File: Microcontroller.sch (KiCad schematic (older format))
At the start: 5 parts

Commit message: added jtag programming header for uC
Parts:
- added J?: Conn_02x03_Counter_Clockwise, symbol Connector_Generic:Conn_02x03_Counter_Clockwise
- added U?: STM32F446VET6-sternie, symbol engine_controller_series3-rescue:STM32F446VET6-sternie
- added U?: OSCILLATOR-sternie, symbol engine_controller_series3-rescue:OSCILLATOR-sternie
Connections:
- net labels added: +3V3, GND, NRST, SW0, SWCLK, SWDIO
- wire segments 15 -> 23
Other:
- note added: "Programming Header\n"
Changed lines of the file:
@@
 EESchema Schematic File Version 4
-LIBS:bangbang_rev1-cache
 EELAYER 30 0
 EELAYER END
 $Descr A4 11693 8268
 encoding utf-8
-Sheet 5 10
+Sheet 7 10
 Title ""
 Date ""
@@
 L engine_controller_series3-rescue:STM32F446VET6-sternie U?
 U 1 1 5E534371
-P 2850 1950
-F 0 "U?" H 2458 2213 49  0000 C CNN
-F 1 "STM32F446VET6-sternie" H 2458 2123 49  0000 C CNN
-F 2 "" H 2000 1000 49  0001 C CNN
-F 3 "" H 2000 1000 49  0001 C CNN
-	1    2850 1950
+P 1750 1300
+F 0 "U?" H 1358 1563 49  0000 C CNN
+F 1 "STM32F446VET6-sternie" H 1358 1473 49  0000 C CNN
+F 2 "" H 900 350 49  0001 C CNN
+F 3 "" H 900 350 49  0001 C CNN
+	1    1750 1300
 	1    0    0    -1
 $EndComp
@@
 L engine_controller_series3-rescue:STM32F446VET6-sternie U?
 U 2 1 5E53758A
-P 5400 2000
-F 0 "U?" H 5033 2263 49  0000 C CNN
-F 1 "STM32F446VET6-sternie" H 5033 2173 49  0000 C CNN
-F 2 "" H 4550 1050 49  0001 C CNN
-F 3 "" H 4550 1050 49  0001 C CNN
-	2    5400 2000
+P 4300 1350
+F 0 "U?" H 3933 1613 49  0000 C CNN
+F 1 "STM32F446VET6-sternie" H 3933 1523 49  0000 C CNN
+F 2 "" H 3450 400 49  0001 C CNN
+F 3 "" H 3450 400 49  0001 C CNN
+	2    4300 1350
 	1    0    0    -1
 $EndComp
@@
 L engine_controller_series3-rescue:STM32F446VET6-sternie U?
 U 3 1 5E53B3C0
-P 2950 4450
-F 0 "U?" H 2483 4713 49  0000 C CNN
-F 1 "STM32F446VET6-sternie" H 2483 4623 49  0000 C CNN
-F 2 "" H 2100 3500 49  0001 C CNN
-F 3 "" H 2100 3500 49  0001 C CNN
-	3    2950 4450
+P 1850 3800
+F 0 "U?" H 1383 4063 49  0000 C CNN
+F 1 "STM32F446VET6-sternie" H 1383 3973 49  0000 C CNN
+F 2 "" H 1000 2850 49  0001 C CNN
+F 3 "" H 1000 2850 49  0001 C CNN
+	3    1850 3800
 	1    0    0    -1
 $EndComp
@@
 L engine_controller_series3-rescue:STM32F446VET6-sternie U?
 U 4 1 5E53EB96
-P 5300 4400
-F 0 "U?" H 5008 4663 49  0000 C CNN
-F 1 "STM32F446VET6-sternie" H 5008 4573 49  0000 C CNN
-F 2 "" H 4450 3450 49  0001 C CNN
-F 3 "" H 4450 3450 49  0001 C CNN
-	4    5300 4400
+P 4200 3750
+F 0 "U?" H 3908 4013 49  0000 C CNN
+F 1 "STM32F446VET6-sternie" H 3908 3923 49  0000 C CNN
+F 2 "" H 3350 2800 49  0001 C CNN
+F 3 "" H 3350 2800 49  0001 C CNN
+	4    4200 3750
 	1    0    0    -1
 $EndComp
@@
 L engine_controller_series3-rescue:STM32F446VET6-sternie U?
 U 5 1 5E54171C
-P 7550 1900
-F 0 "U?" H 7258 2163 49  0000 C CNN
-F 1 "STM32F446VET6-sternie" H 7258 2073 49  0000 C CNN
-F 2 "" H 6700 950 49  0001 C CNN
-F 3 "" H 6700 950 49  0001 C CNN
-	5    7550 1900
-	1    0    0    -1
-$EndComp
-Text GLabel 3050 2450 2    50   Input ~ 0
+P 6300 1400
+F 0 "U?" H 6008 1663 49  0000 C CNN
+F 1 "STM32F446VET6-sternie" H 6008 1573 49  0000 C CNN
+F 2 "" H 5450 450 49  0001 C CNN
+F 3 "" H 5450 450 49  0001 C CNN
+	5    6300 1400
+	1    0    0    -1
+$EndComp
+Text GLabel 1950 1800 2    50   Input ~ 0
 SPI1_SCK
-Text GLabel 3050 2550 2    50   Input ~ 0
+Text GLabel 1950 1900 2    50   Input ~ 0
 SPI1_MISO
-Text GLabel 3050 2650 2    50   Input ~ 0
+Text GLabel 1950 2000 2    50   Input ~ 0
 SPI1_MOSI
 Wire Wire Line
-	2850 2450 3050 2450
-Wire Wire Line
-	2850 2550 3050 2550
-Wire Wire Line
-	2850 2650 3050 2650
-Text GLabel 3050 2950 2    50   Input ~ 0
+	1750 1800 1950 1800
+Wire Wire Line
+	1750 1900 1950 1900
+Wire Wire Line
+	1750 2000 1950 2000
+Text GLabel 1950 2300 2    50   Input ~ 0
 en_vlv0
-Text GLabel 3050 3050 2    50   Input ~ 0
+Text GLabel 1950 2400 2    50   Input ~ 0
 en_vlv1
 Wire Wire Line
-	2850 2950 3050 2950
-Wire Wire Line
-	2850 3050 3050 3050
-Text GLabel 3150 5050 2    50   Input ~ 0
+	1750 2300 1950 2300
+Wire Wire Line
+	1750 2400 1950 2400
+Text GLabel 2050 4400 2    50   Input ~ 0
 Mtr1_pwm
 Wire Wire Line
-	3150 5050 2950 5050
-Text GLabel 5600 2300 2    50   Input ~ 0
+	2050 4400 1850 4400
+Text GLabel 4500 1650 2    50   Input ~ 0
 Mtr0_B_L
-Text GLabel 5600 2400 2    50   Input ~ 0
+Text GLabel 4500 1750 2    50   Input ~ 0
 Mtr0_B_H
-Text GLabel 5600 2500 2    50   Input ~ 0
+Text GLabel 4500 1850 2    50   Input ~ 0
 Mtr0_A_L
-Text GLabel 5600 2600 2    50   Input ~ 0
+Text GLabel 4500 1950 2    50   Input ~ 0
 Mtr0_A_H
 Wire Wire Line
-	5400 2300 5600 2300
-Wire Wire Line
-	5400 2400 5600 2400
-Wire Wire Line
-	5400 2500 5600 2500
-Wire Wire Line
-	5400 2600 5600 2600
-Text GLabel 5550 4500 2    50   Input ~ 0
+	4300 1650 4500 1650
+Wire Wire Line
+	4300 1750 4500 1750
+Wire Wire Line
+	4300 1850 4500 1850
+Wire Wire Line
+	4300 1950 4500 1950
+Text GLabel 4450 3850 2    50   Input ~ 0
 Mtr1_B_L
-Text GLabel 5550 4600 2    50   Input ~ 0
+Text GLabel 4450 3950 2    50   Input ~ 0
 Mtr1_B_H
-Text GLabel 5550 4700 2    50   Input ~ 0
+Text GLabel 4450 4050 2    50   Input ~ 0
 Mtr1_A_L
-Text GLabel 5550 4800 2    50   Input ~ 0
+Text GLabel 4450 4150 2    50   Input ~ 0
 Mtr1_A_H
 Wire Wire Line
-	5300 4500 5550 4500
-Wire Wire Line
-	5550 4600 5300 4600
-Wire Wire Line
-	5300 4700 5550 4700
-Wire Wire Line
-	5550 4800 5300 4800
-Text GLabel 7750 2800 2    50   Input ~ 0
+	4200 3850 4450 3850
+Wire Wire Line
+	4450 3950 4200 3950
+Wire Wire Line
+	4200 4050 4450 4050
+Wire Wire Line
+	4450 4150 4200 4150
+Text GLabel 6500 2300 2    50   Input ~ 0
 Mtr0_pwm
 Wire Wire Line
-	7550 2800 7750 2800
+	6300 2300 6500 2300
+Text Notes 7000 5400 0    123  ~ 25
+Programming Header\n
+$Comp
+L Connector_Generic:Conn_02x03_Counter_Clockwise J?
+U 1 1 5E5320E3
+P 7900 5950
+F 0 "J?" H 7950 6267 50  0000 C CNN
+F 1 "Conn_02x03_Counter_Clockwise" H 7950 6176 50  0000 C CNN
+F 2 "" H 7900 5950 50  0001 C CNN
+F 3 "~" H 7900 5950 50  0001 C CNN
+	1    7900 5950
+	1    0    0    -1
+$EndComp
+Text GLabel 8300 5850 2    50   Input ~ 0
+SW0
+Text GLabel 7550 5850 0    50   Input ~ 0
+SWDIO
+Text GLabel 7550 5950 0    50   Input ~ 0
+SWCLK
+Text GLabel 7550 6050 0    50   Input ~ 0
+NRST
+Wire Wire Line
+	7550 5850 7700 5850
+Wire Wire Line
+	7700 5950 7550 5950
+Wire Wire Line
+	7550 6050 7700 6050
+Wire Wire Line
+	8200 5850 8300 5850
+Wire Wire Line
+	8200 5950 8650 5950
+Wire Wire Line
+	8650 5950 8650 5700
+Wire Wire Line
+	8200 6050 8450 6050
+Wire Wire Line
+	8450 6050 8450 6150
+$Comp
+L power:+3V3 #PWR?
+U 1 1 5E5398EA
+P 8650 5700
+F 0 "#PWR?" H 8650 5550 50  0001 C CNN
+F 1 "+3V3" H 8665 5873 50  0000 C CNN
+F 2 "" H 8650 5700 50  0001 C CNN
+F 3 "" H 8650 5700 50  0001 C CNN
+	1    8650 5700
+	1    0    0    -1
+$EndComp
+$Comp
+L power:GND #PWR?
+U 1 1 5E53A4AC
+P 8450 6150
+F 0 "#PWR?" H 8450 5900 50  0001 C CNN
+F 1 "GND" H 8455 5977 50  0000 C CNN
+F 2 "" H 8450 6150 50  0001 C CNN
+F 3 "" H 8450 6150 50  0001 C CNN
+	1    8450 6150
+	1    0    0    -1
+$EndComp
+$Comp
+L engine_controller_series3-rescue:STM32F446VET6-sternie U?
+U 6 1 5E53BC0E
+P 9700 3050
+F 0 "U?" H 9675 3763 49  0000 C CNN
+F 1 "STM32F446VET6-sternie" H 9675 3673 49  0000 C CNN
+F 2 "" H 8850 2100 49  0001 C CNN
+F 3 "" H 8850 2100 49  0001 C CNN
+	6    9700 3050
+	1    0    0    -1
+$EndComp
+Text GLabel 8900 2950 0    50   Input ~ 0
+NRST
+$Comp
+L engine_controller_series3-rescue:OSCILLATOR-sternie U?
+U 1 1 5E54009F
+P 7550 3600
+F 0 "U?" H 7550 3966 118 0000 C CNN
+F 1 "OSCILLATOR-sternie" H 7550 3824 50  0000 C CNN
+F 2 "" H 7550 3600 118 0001 C CNN
+F 3 "" H 7550 3600 118 0001 C CNN
+	1    7550 3600
+	1    0    0    -1
+$EndComp
 $EndSCHEMATC

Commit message: finished up uC sheet and pressure transducers
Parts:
- added B1: Push_Button-sternie, symbol engine_controller_series3-rescue:Push_Button-sternie
- added C? (x2): 2u2, symbol Device:C
- added C? (x11): 100n, symbol Device:C
- added JP?: Jumper, symbol Device:Jumper
- added R?: R, symbol Device:R
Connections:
- net labels added: +3.3V
- wire segments 23 -> 105
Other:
- moved on the sheet: J?

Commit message: Valves and ducers
Finished valves and ducers and their connectors. Got rid of 4 pin ducers. Made all ducers powered by +5V. Cleaned up some uneeded files.
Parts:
- B1: symbol engine_controller_series3-rescue:Push_Button-sternie -> bangbang_rev1-rescue:Push_Button-sternie-engine_controller_series3-rescue
- U? (x6): symbol engine_controller_series3-rescue:STM32F446VET6-sternie -> bangbang_rev1-rescue:STM32F446VET6-sternie-engine_controller_series3-rescue
- U?: symbol engine_controller_series3-rescue:OSCILLATOR-sternie -> bangbang_rev1-rescue:OSCILLATOR-sternie-engine_controller_series3-rescue
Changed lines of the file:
@@
 $EndDescr
 $Comp
-L engine_controller_series3-rescue:STM32F446VET6-sternie U?
+L bangbang_rev1-rescue:STM32F446VET6-sternie-engine_controller_series3-rescue U?
 U 1 1 5E534371
 P 1750 1300
@@
 $EndComp
 $Comp
-L engine_controller_series3-rescue:STM32F446VET6-sternie U?
+L bangbang_rev1-rescue:STM32F446VET6-sternie-engine_controller_series3-rescue U?
 U 2 1 5E53758A
 P 4300 1350
@@
 $EndComp
 $Comp
-L engine_controller_series3-rescue:STM32F446VET6-sternie U?
+L bangbang_rev1-rescue:STM32F446VET6-sternie-engine_controller_series3-rescue U?
 U 3 1 5E53B3C0
 P 1850 3800
@@
 $EndComp
 $Comp
-L engine_controller_series3-rescue:STM32F446VET6-sternie U?
+L bangbang_rev1-rescue:STM32F446VET6-sternie-engine_controller_series3-rescue U?
 U 4 1 5E53EB96
 P 4200 3750
@@
 $EndComp
 $Comp
-L engine_controller_series3-rescue:STM32F446VET6-sternie U?
+L bangbang_rev1-rescue:STM32F446VET6-sternie-engine_controller_series3-rescue U?
 U 5 1 5E54171C
 P 6300 1400
@@
 $EndComp
 $Comp
-L engine_controller_series3-rescue:STM32F446VET6-sternie U?
+L bangbang_rev1-rescue:STM32F446VET6-sternie-engine_controller_series3-rescue U?
 U 6 1 5E53BC0E
 P 9700 3050
@@
 NRST
 $Comp
-L engine_controller_series3-rescue:OSCILLATOR-sternie U?
+L bangbang_rev1-rescue:OSCILLATOR-sternie-engine_controller_series3-rescue U?
 U 1 1 5E54009F
 P 7550 3600
@@
 $EndComp
 $Comp
-L engine_controller_series3-rescue:Push_Button-sternie B1
+L bangbang_rev1-rescue:Push_Button-sternie-engine_controller_series3-rescue B1
 U 1 1 5E641210
 P 9700 5050

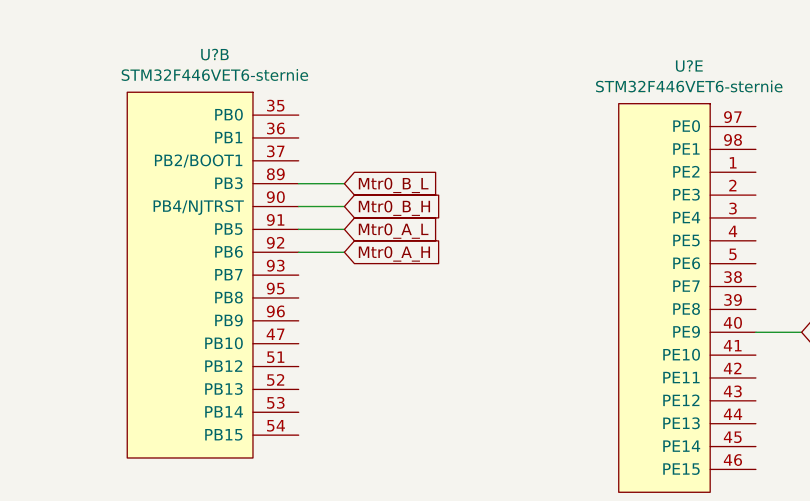
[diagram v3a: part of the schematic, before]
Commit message: Motor channels mostly finished
Todo: Need to determine capacitance of decoupling caps in motor channel.
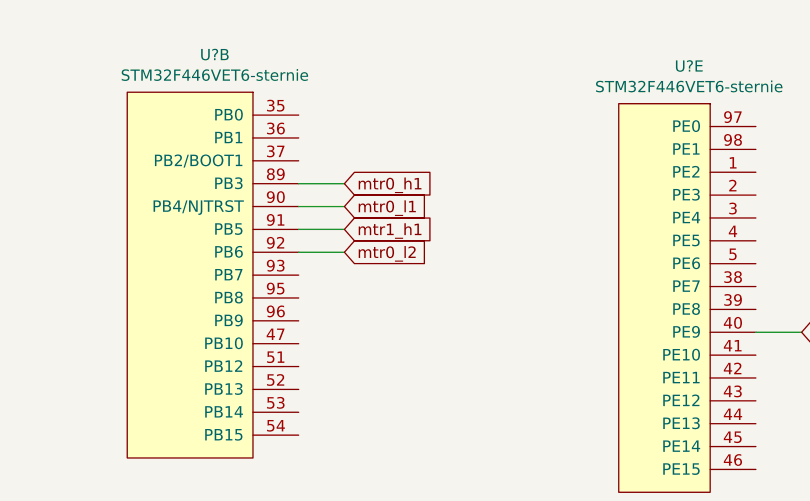
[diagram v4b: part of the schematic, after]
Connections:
- net Mtr0_A_H renamed mtr0_l2
- net Mtr0_A_L renamed mtr1_h1
- net Mtr0_B_H renamed mtr0_l1
- net Mtr0_B_L renamed mtr0_h1
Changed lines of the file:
@@
 $Descr A4 11693 8268
 encoding utf-8
-Sheet 7 11
+Sheet 8 12
 Title ""
 Date ""
@@
 	2050 4400 1850 4400
 Text GLabel 4500 1650 2    50   Input ~ 0
-Mtr0_B_L
+mtr0_h1
 Text GLabel 4500 1750 2    50   Input ~ 0
-Mtr0_B_H
-Text GLabel 4500 1850 2    50   Input ~ 0
-Mtr0_A_L
-Text GLabel 4500 1950 2    50   Input ~ 0
-Mtr0_A_H
+mtr0_l1
 Wire Wire Line
 	4300 1650 4500 1650
@@
 	1    0    0    -1
 $EndComp
+Text GLabel 4500 1850 2    50   Input ~ 0
+mtr1_h1
+Text GLabel 4500 1950 2    50   Input ~ 0
+mtr0_l2
 $EndSCHEMATC

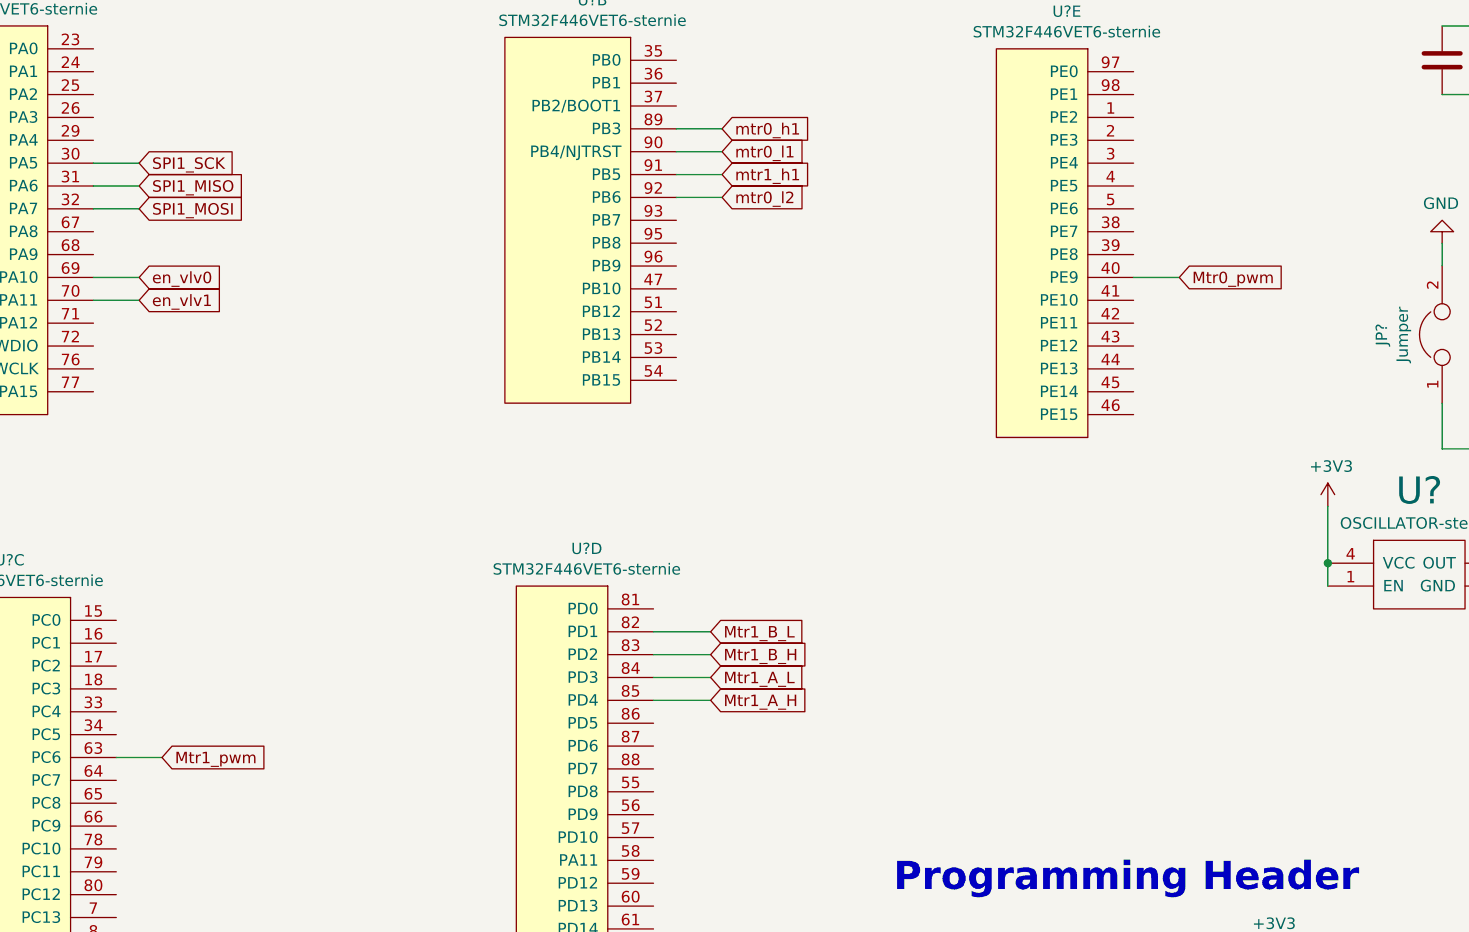
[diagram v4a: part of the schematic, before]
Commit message: hotfix
fixed some labels
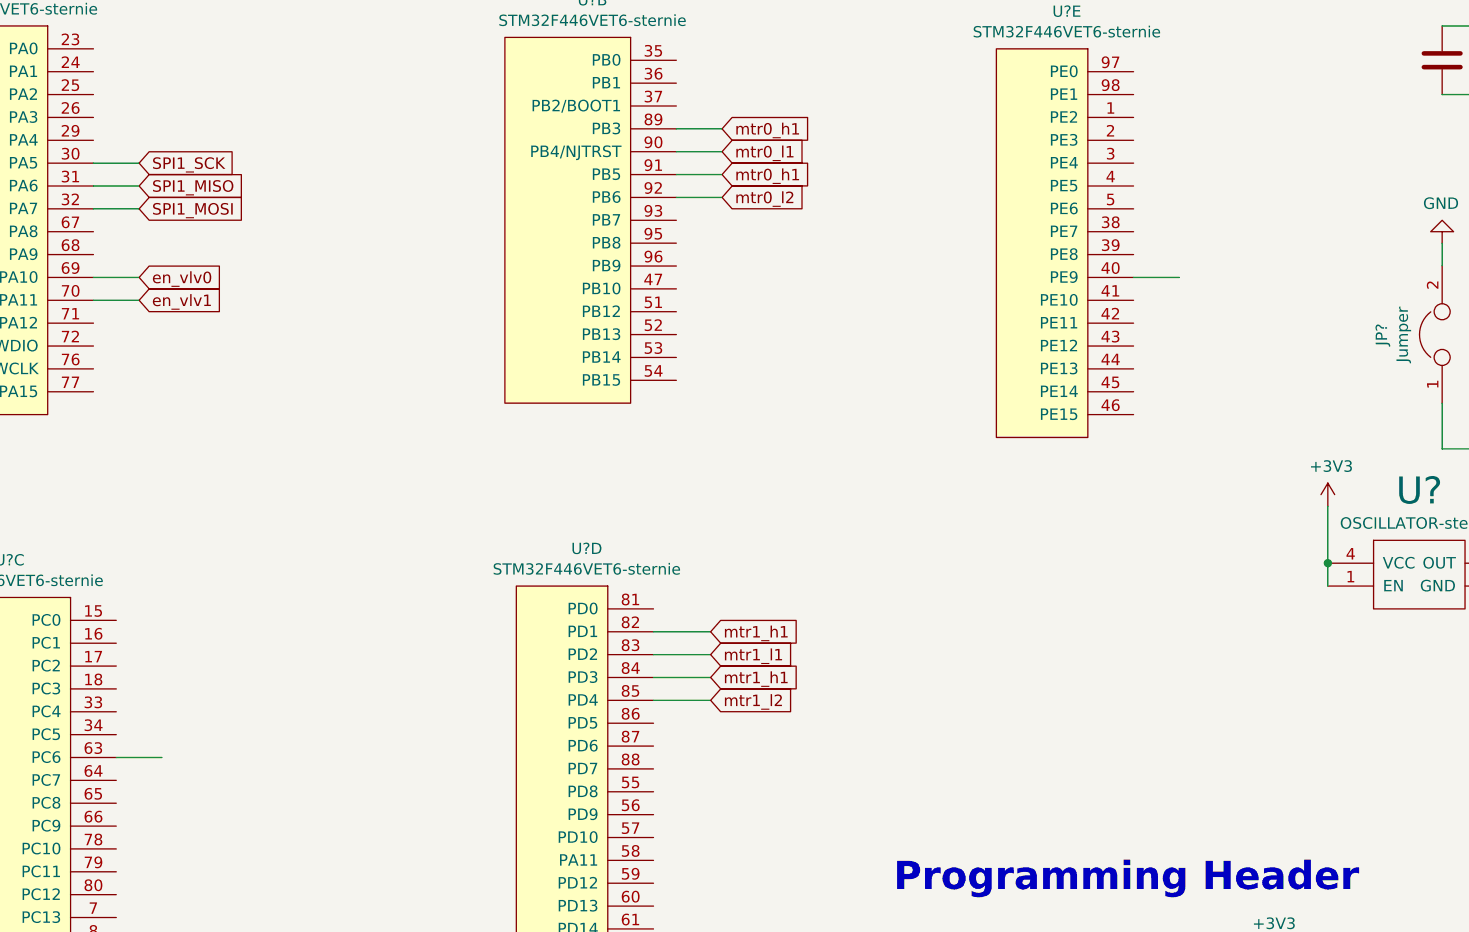
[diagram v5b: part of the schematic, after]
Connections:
- net labels added: mtr1_l1, mtr1_l2
- net labels removed: Mtr0_pwm, Mtr1_A_H, Mtr1_A_L, Mtr1_B_H, Mtr1_B_L, Mtr1_pwm
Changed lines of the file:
@@
 Wire Wire Line
 	1750 2400 1950 2400
-Text GLabel 2050 4400 2    50   Input ~ 0
-Mtr1_pwm
 Wire Wire Line
 	2050 4400 1850 4400
@@
 Wire Wire Line
 	4300 1950 4500 1950
-Text GLabel 4450 3850 2    50   Input ~ 0
-Mtr1_B_L
-Text GLabel 4450 3950 2    50   Input ~ 0
-Mtr1_B_H
-Text GLabel 4450 4050 2    50   Input ~ 0
-Mtr1_A_L
-Text GLabel 4450 4150 2    50   Input ~ 0
-Mtr1_A_H
 Wire Wire Line
 	4200 3850 4450 3850
@@
 Wire Wire Line
 	4450 4150 4200 4150
-Text GLabel 6500 2300 2    50   Input ~ 0
-Mtr0_pwm
 Wire Wire Line
 	6300 2300 6500 2300
@@
 $EndComp
 Text GLabel 4500 1850 2    50   Input ~ 0
-mtr1_h1
+mtr0_h1
 Text GLabel 4500 1950 2    50   Input ~ 0
 mtr0_l2
+Text GLabel 4450 3850 2    50   Input ~ 0
+mtr1_h1
+Text GLabel 4450 3950 2    50   Input ~ 0
+mtr1_l1
+Text GLabel 4450 4050 2    50   Input ~ 0
+mtr1_h1
+Text GLabel 4450 4150 2    50   Input ~ 0
+mtr1_l2
 $EndSCHEMATC
